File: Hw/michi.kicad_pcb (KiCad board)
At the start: 2 copper layers, 93.9 x 120.8 mm, 57 parts, among them J1 Conn_01x02, J2 Conn_Right, P1 USB_C_Plug_USB2.0, P6 D, SW1 SW_Push, U1 RP2040, U2 NCP1117ST33T3G, U3 W25Q128JVS, Y1 Crystal

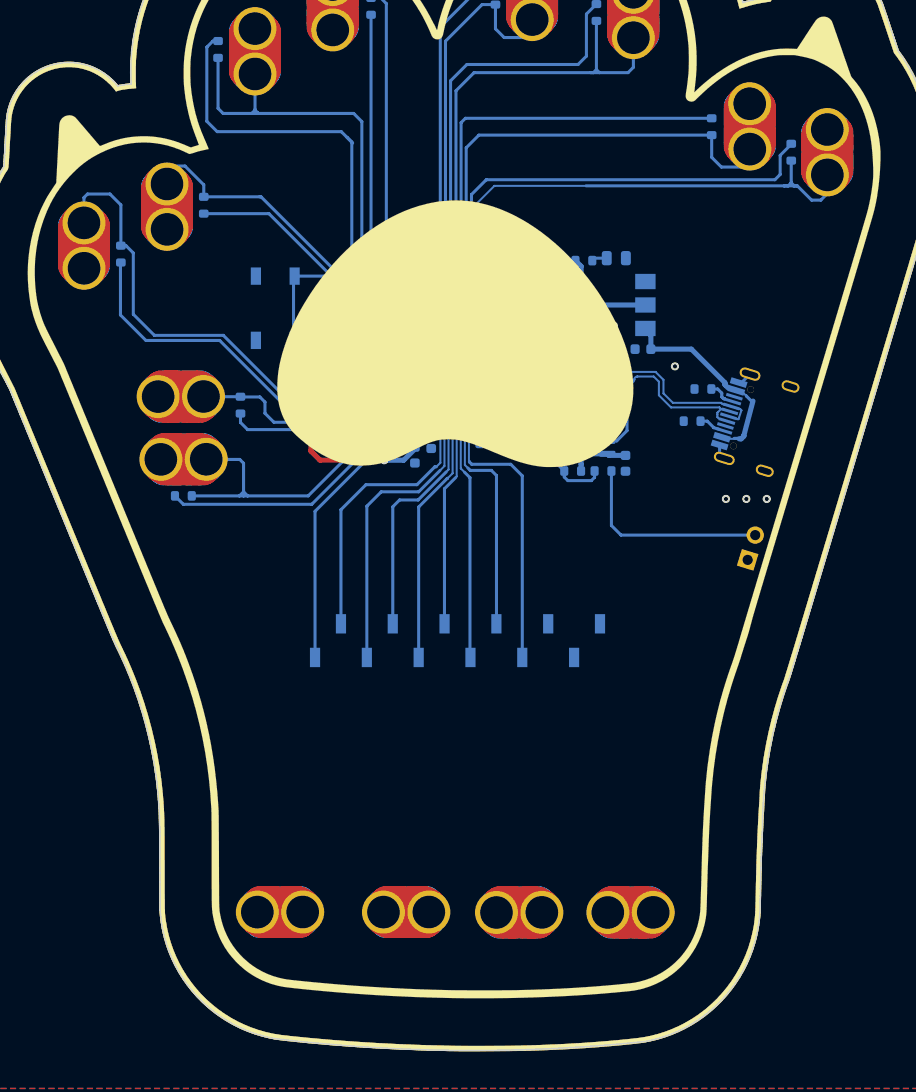
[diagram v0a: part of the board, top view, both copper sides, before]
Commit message: Add labels
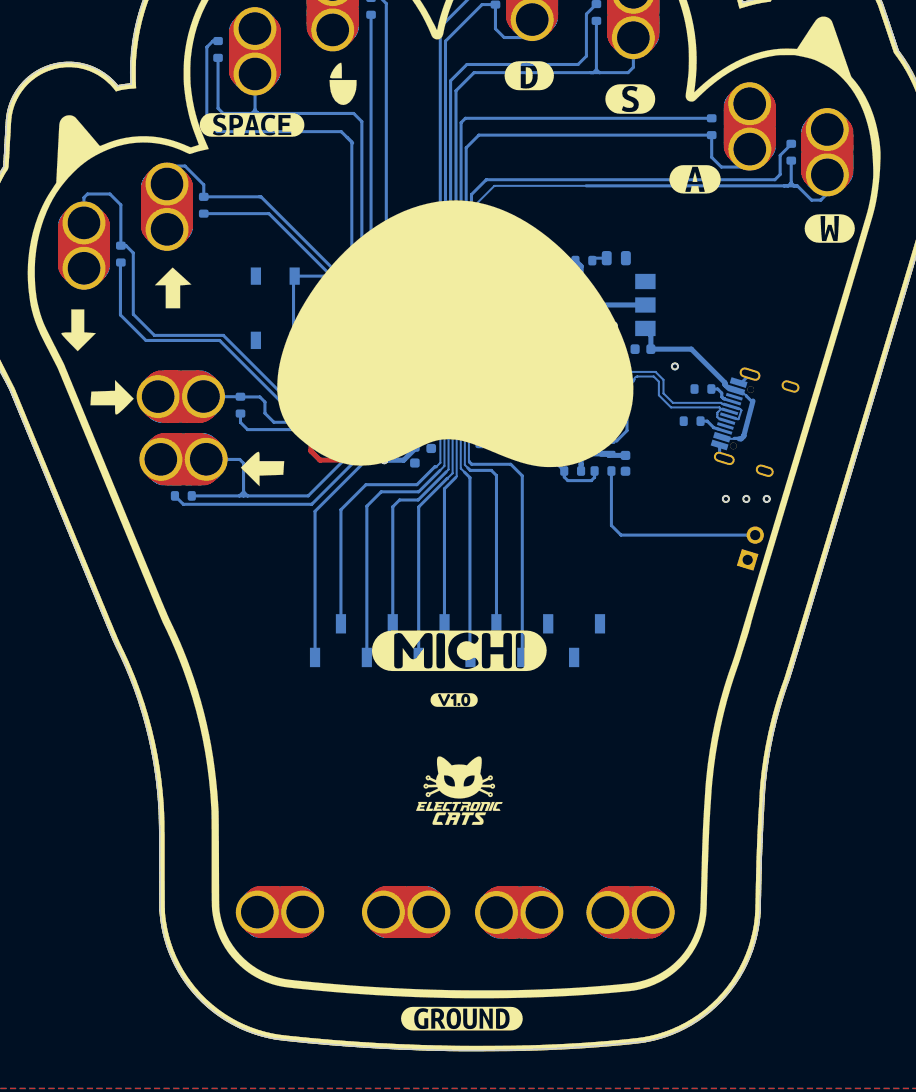
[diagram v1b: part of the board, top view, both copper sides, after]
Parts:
- added G***: LOGO, LOGO, F.Cu at (83.8, 95.2)
- added G***: LOGO, LOGO, B.Cu at (106.4, 64.3)
- added G***: LOGO, LOGO, B.Cu at (98.6, 101.9)
- added G***: LOGO, Aesthetics:electronic_cats_logo_8x6, B.Cu at (94.2, 116.1)
- added G***: LOGO, LOGO, B.Cu at (83.6, 95.2)
- added G***: LOGO, Aesthetics:electronic_cats_logo_8x6, F.Cu at (117.9, 133.6)
- added G***: LOGO, LOGO, F.Cu at (89.9, 84.3)
- added G***: LOGO, LOGO, F.Cu at (98.6, 101.9)
- added G***: LOGO, LOGO, F.Cu at (106.4, 64.3)
- added G***: LOGO, LOGO, F.Cu at (80.5, 88.4)
- added G***: LOGO, LOGO, B.Cu at (99.8, 78.7)
- added G***: LOGO, LOGO, B.Cu at (89.9, 84.3)
- added G***: LOGO, LOGO, B.Cu at (80.5, 88.4)
- added kibuzzard-63055E62: G***, kibuzzard-63055E62, F.Cu at (141.0, 73.7)
- added kibuzzard-63055E62: G***, kibuzzard-63055E62, B.Cu at (141.0, 73.7)
- added kibuzzard-63055E6D: G***, kibuzzard-63055E6D, F.Cu at (154.2, 78.5)
- added kibuzzard-63055E6D: G***, kibuzzard-63055E6D, B.Cu at (154.2, 78.5)
- added kibuzzard-63055E8E: G***, kibuzzard-63055E8E, F.Cu at (124.7, 63.5)
- added kibuzzard-63055E8E: G***, kibuzzard-63055E8E, B.Cu at (124.7, 63.5)
- added kibuzzard-63055EA5: G***, kibuzzard-63055EA5, F.Cu at (97.5, 68.3)
- added kibuzzard-63055EA5: G***, kibuzzard-63055EA5, B.Cu at (97.5, 68.3)
- added kibuzzard-63055F28: G***, kibuzzard-63055F28, F.Cu at (118.1, 156.0)
- added kibuzzard-63055F28: G***, kibuzzard-63055F28, B.Cu at (118.1, 156.0)
- added kibuzzard-63055FE6: G***, kibuzzard-63055FE6, F.Cu at (134.6, 65.8)
- added kibuzzard-63055FE6: G***, kibuzzard-63055FE6, B.Cu at (134.6, 65.8)
- added kibuzzard-630561F0: G***, kibuzzard-630561F0, B.Cu at (106.2, 125.7)
- added kibuzzard-63056210: G***, kibuzzard-63056210, B.Cu at (103.6, 125.7)
- added kibuzzard-6305622D: G***, kibuzzard-6305622D, B.Cu at (108.7, 112.3)
- added kibuzzard-6305624B: G***, kibuzzard-6305624B, B.Cu at (111.3, 112.3)
- added kibuzzard-63056260: G***, kibuzzard-63056260, B.Cu at (113.8, 125.5)
- added kibuzzard-63056270: G***, kibuzzard-63056270, B.Cu at (121.4, 112.8)
- added kibuzzard-63056280: G***, kibuzzard-63056280, B.Cu at (124.0, 112.8)
- added kibuzzard-63056299: G***, kibuzzard-63056299, B.Cu at (118.9, 123.4)
- added kibuzzard-630562A3: G***, kibuzzard-630562A3, B.Cu at (131.6, 113.8)
- added kibuzzard-630562A3: G***, kibuzzard-630562A3, B.Cu at (126.5, 113.8)
- added kibuzzard-630562A3: G***, kibuzzard-630562A3, B.Cu at (129.0, 113.8)
- added kibuzzard-630562BF: G***, kibuzzard-630562BF, B.Cu at (116.3, 123.4)
- added kibuzzard-6305640E: G***, kibuzzard-6305640E, F.Cu at (117.9, 119.9)
- added kibuzzard-6305642C: G***, kibuzzard-6305642C, F.Cu at (117.3, 124.7)
- added svg2mod: G***, Aesthetics:usb_graphic, B.Cu at (150.6, 90.7)

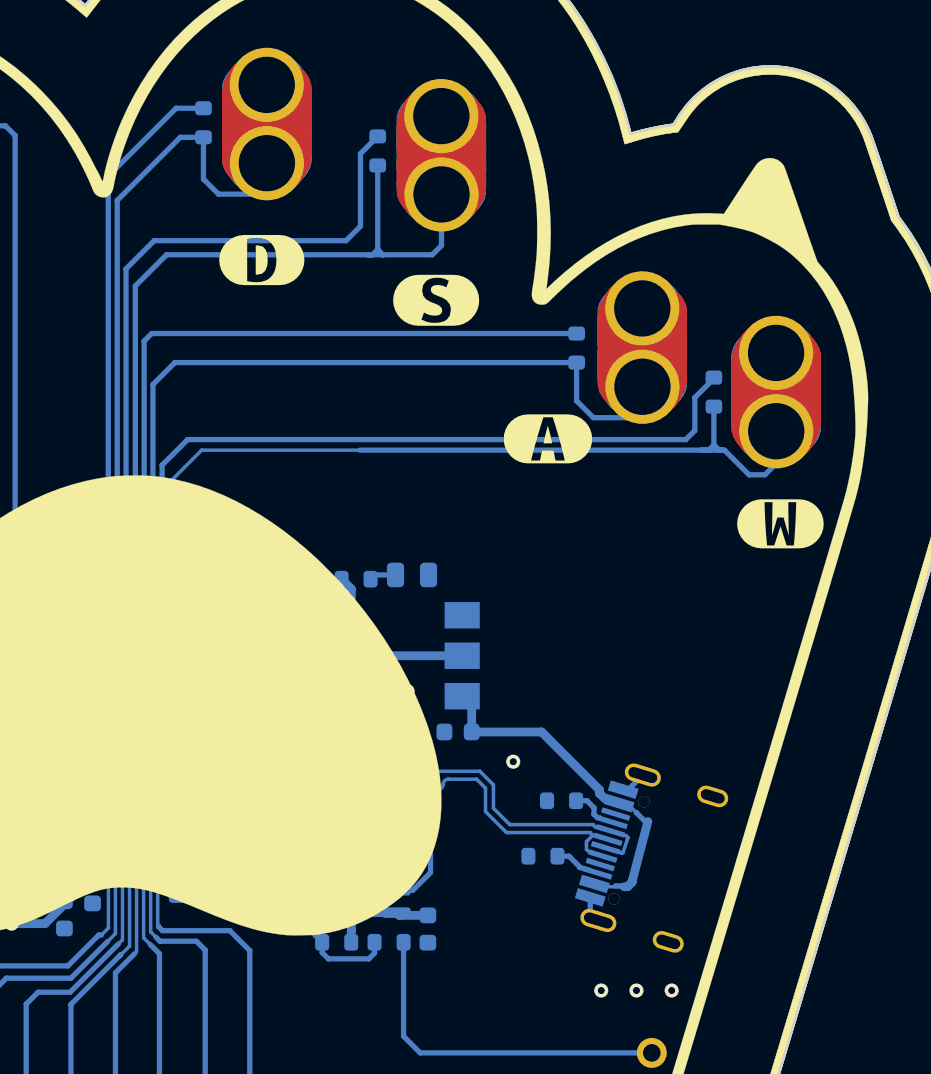
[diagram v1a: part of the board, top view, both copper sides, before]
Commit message: fix footprints
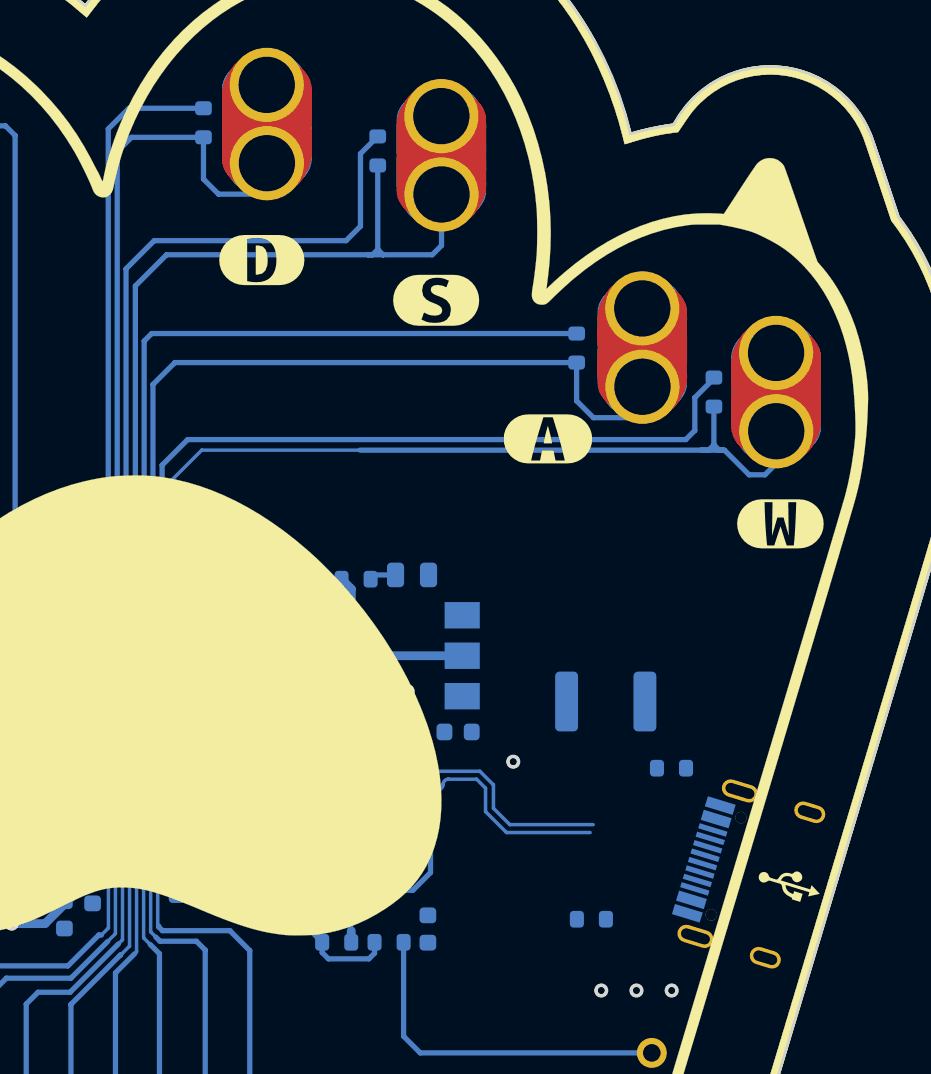
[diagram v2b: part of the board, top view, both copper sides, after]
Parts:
- added F1: 0.5A, Fuse:Fuse_1812_4532Metric_Pad1.30x3.40mm_HandSolder, B.Cu at (144.3, 88.6)
- added svg2mod: G***, Aesthetics:usb_graphic, F.Cu at (154.7, 98.9)
- U3: footprint Package_SO:SOIC-8_5.23x5.23mm_P1.27mm -> Library:W25Q16JVUUIQ
- moved R1 6.51 mm to (148.0, 92.4)
- moved svg2mod 5.74 mm to (156.1, 92.5), turned to 73 degrees
- moved P1 5.59 mm to (150.6, 97.8)
- moved R2 4.52 mm to (143.4, 101.0)
- moved U3 1.39 mm to (127.5, 98.1), turned to 90 degrees
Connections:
- P1 pad A4: VBUS -> Net-(P1-PadA4)
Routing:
- net VBUS: track 20.8 -> 0.00 mm
- net +3V3: track 106.8 -> 87.1 mm, vias 4 -> 3
- net GND: track 10.0 -> 7.07 mm
- net /D-: track 24.2 -> 21.7 mm
- net Net-(P1-PadB5): track 2.13 -> 0.00 mm
- net Net-(P1-PadA5): track 1.95 -> 0.00 mm
- net /D+: track 24.0 -> 22.1 mm
- net /IO23: track 42.9 -> 44.5 mm
- net /IO22: track 37.3 -> 38.8 mm

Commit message: Resize
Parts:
- added Ref**: Val**, PCB_Michi_Act, F.Cu at (27.9, 104.4)

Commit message: update v1.0 layout
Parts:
- removed the G*** at (98.6, 101.9)
- removed the G*** at (83.6, 95.2)
- removed the G*** at (89.9, 84.3)
- removed the G*** at (80.5, 88.4)
- removed the P6 at (90.4, 94.9)
- removed R13: DNP, Resistor_SMD:R_0603_1608Metric
- removed R21: 10k, Resistor_SMD:R_0603_1608Metric
- removed the Ref** at (117.4, 98.7)
- removed the kibuzzard-63055F28 at (118.1, 156.0)
- added G***: LOGO, LOGO, B.Cu at (112.0, 109.8)
- added G***: LOGO, LOGO, B.Cu at (115.7, 109.8)
- added G***: LOGO, LOGO, B.Cu at (114.0, 111.5)
- added G***: LOGO, LOGO, B.Cu at (113.7, 108.1)
- added P6: D, SEWALLI_renew, F.Cu at (132.0, 137.1)
- added P6: D, SEWALLI_renew, F.Cu at (106.0, 125.0)
- Ref**: moved to B.Cu
- moved Ref** 90.3 mm to (117.9, 97.0), turned to 180 degrees
- moved svg2mod 73.6 mm to (82.8, 84.8), turned to -73 degrees
- moved svg2mod 73.1 mm to (82.9, 85.0), turned to 107 degrees
- moved kibuzzard-63056210 64.6 mm to (134.0, 68.7), turned to 90 degrees
- moved kibuzzard-63055EA5 63.2 mm to (137.5, 117.3), turned to -90 degrees
- moved P6 62.3 mm to (123.0, 118.0)
- moved P1 62.1 mm to (89.1, 89.7), turned to 107 degrees
- moved kibuzzard-630561F0 61.9 mm to (130.1, 68.6), turned to 90 degrees
- moved J1 58.9 mm to (87.9, 101.9), turned to -163 degrees
- moved kibuzzard-63056260 58.7 mm to (122.3, 67.4), turned to 90 degrees
- moved G*** 57.2 mm to (127.6, 117.5)
- moved kibuzzard-63055EA5 55.4 mm to (132.9, 111.0)
- moved kibuzzard-630562BF 54.3 mm to (119.6, 69.2)
- moved kibuzzard-63056299 54.3 mm to (117.2, 69.2)
- moved R2 53.8 mm to (92.0, 85.4), turned to 107 degrees
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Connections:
- D1 pad 1: GND -> /IO15
- J2 pad 10: GND -> +3V3
- P6 pad 1: /IO25 -> /IO14
- P6 pad : (no net) -> /IO10
- P6 pad 1: /IO21 -> /IO10
- P6 pad 1: /IO27 -> /IO17
- P6 pad 1: /IO23 -> /IO12
- P6 pad 1: /IO29 -> /IO19
- P6 pad 1: /IO10 -> /IO27
- P6 pad 1: /IO14 -> /IO23
- P6 pad 1: /IO17 -> /IO29
- P6 pad 1: /IO19 -> /IO21
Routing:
- net GND: track 7.07 -> 98.1 mm, vias 19 -> 27
- net /IO10: track 35.1 -> 87.8 mm
- net /IO12: track 23.6 -> 70.1 mm
- net /IO17: track 33.2 -> 68.7 mm
- net /SS: track 16.4 -> 50.8 mm, vias 0 -> 2
- net /IO18: track 46.2 -> 12.1 mm
- net /IO24: track 44.9 -> 11.6 mm
- net /IO28: track 48.6 -> 16.3 mm
- net /IO26: track 45.8 -> 13.6 mm
- net /IO22: track 38.8 -> 9.46 mm
- net +3V3: track 87.1 -> 116.4 mm, vias 3 -> 8
- net /IO27: track 50.8 -> 23.4 mm
- net /IO13: track 39.2 -> 13.8 mm
- net /IO9: track 29.7 -> 8.00 mm
- net /IO20: track 33.8 -> 13.7 mm
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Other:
- board size 93.9 x 120.8 mm -> 80 x 102.8 mm

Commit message: fix label VCC 3v3
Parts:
- removed the kibuzzard-630562A3 at (109.5, 68.6)
- added kibuzzard-639765AD: G***, kibuzzard-639765AD, B.Cu at (109.0, 68.1)
- added kibuzzard-639765C9: G***, kibuzzard-639765C9, B.Cu at (91.4, 107.2)

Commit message: label v1.1
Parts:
- removed kibuzzard-6305642C: G***, kibuzzard-6305642C
- added kibuzzard-6449595B: G***, kibuzzard-6449595B, F.Cu at (102.2, 85.1)
